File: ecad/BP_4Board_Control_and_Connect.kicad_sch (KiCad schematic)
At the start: 10 parts, among them U40 TCA9544APWR, U41 CD4051BPWR4, U42 CD4051BPWR4

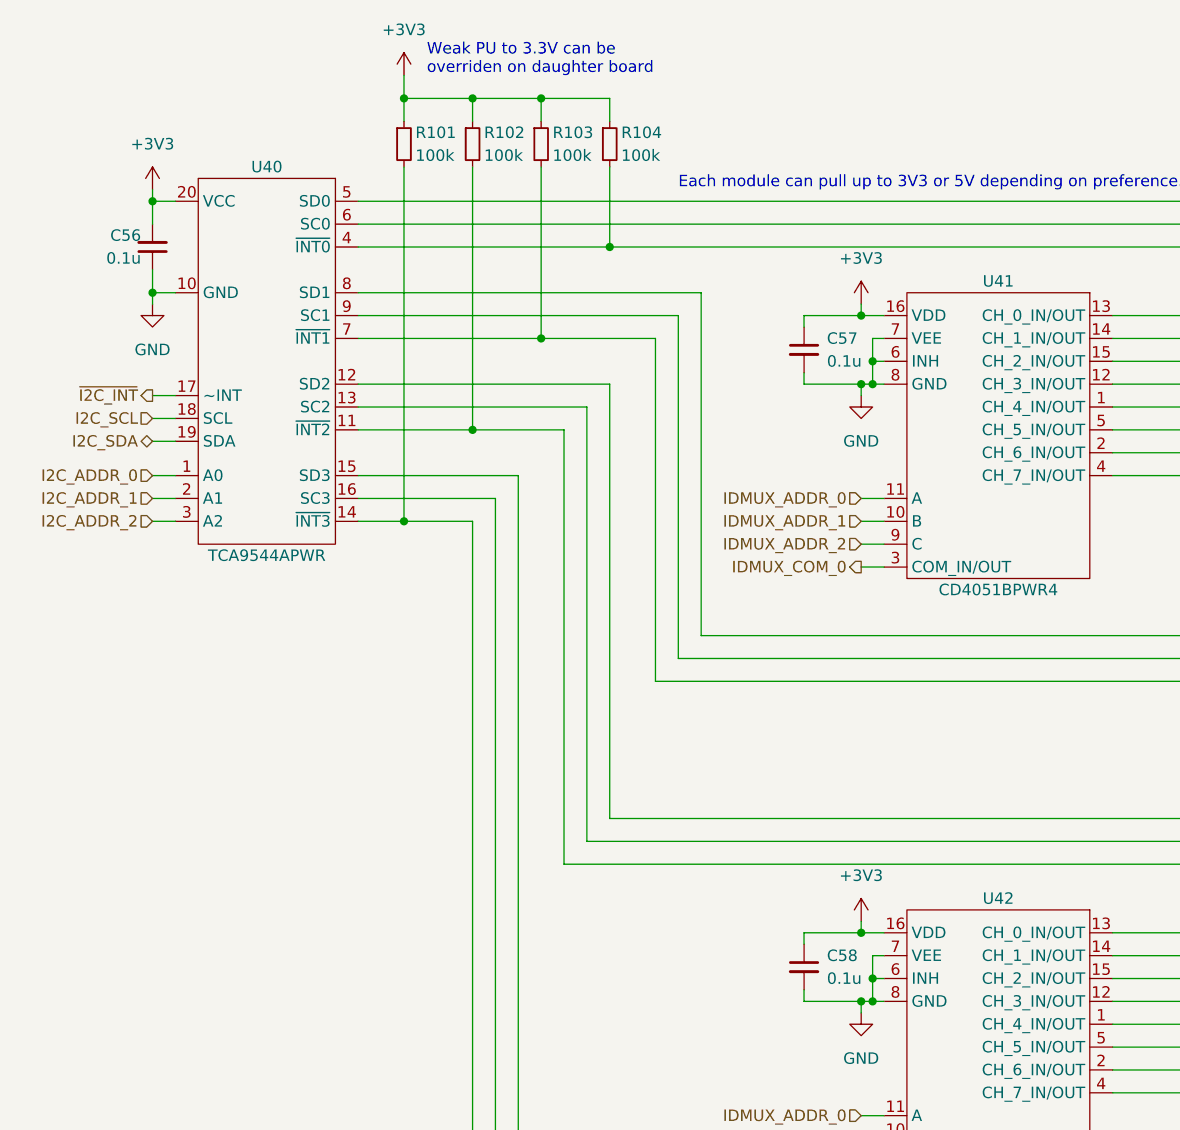
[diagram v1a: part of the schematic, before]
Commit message: Fixes to footprint numbering in multi-unit parts.
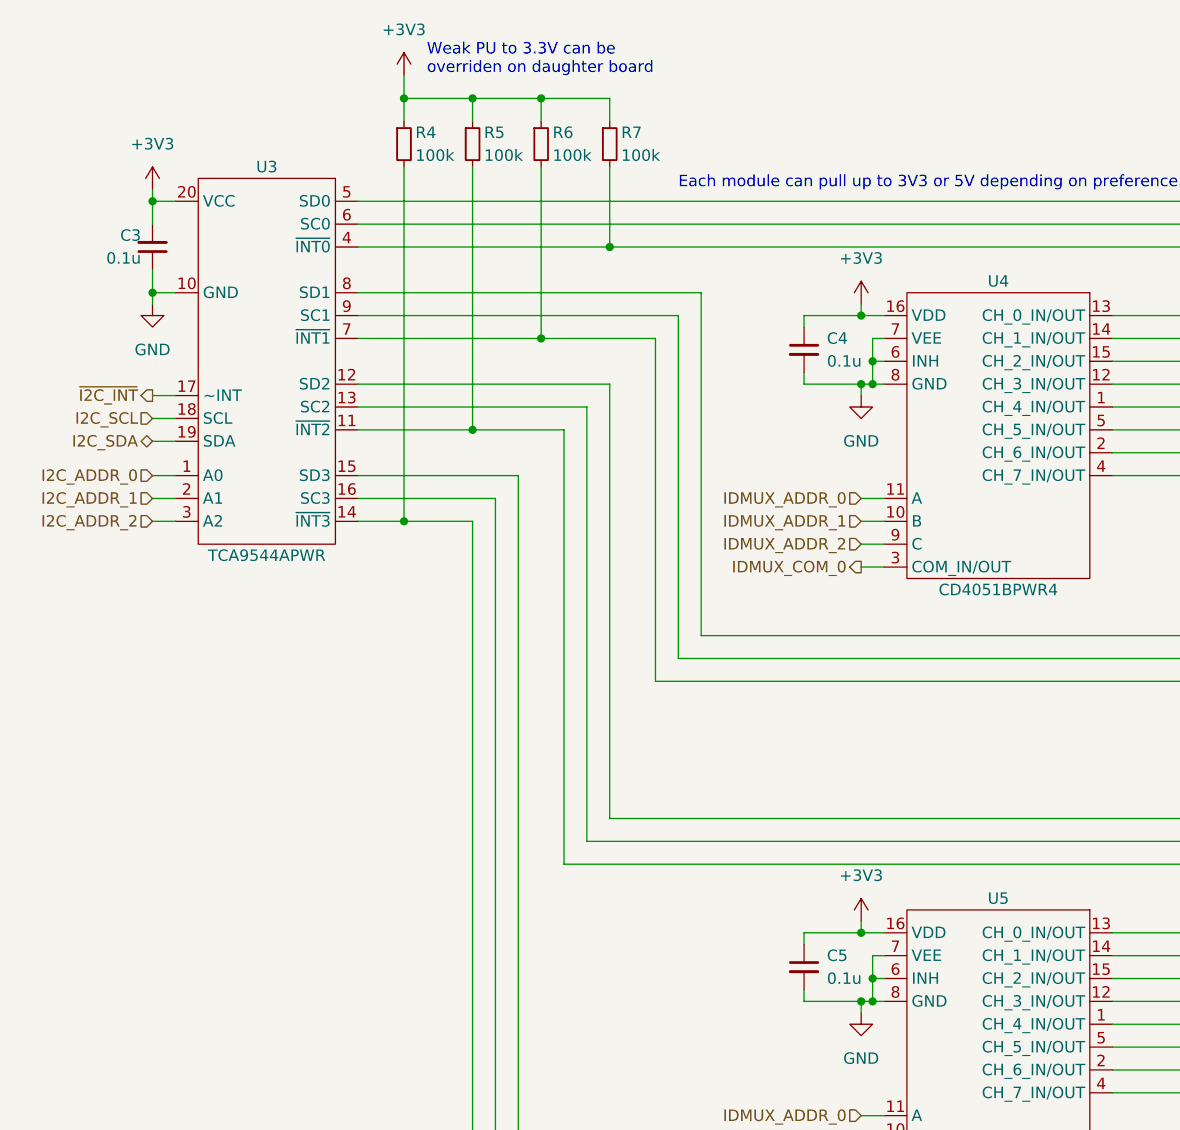
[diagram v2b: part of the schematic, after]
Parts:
- renumbered C56 to C3, C57 to C4, C58 to C5, R101 to R4, R102 to R5, R103 to R6, R104 to R7, U40 to U3, U41 to U4, U42 to U5
